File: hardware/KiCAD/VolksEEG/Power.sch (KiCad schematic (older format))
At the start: 43 parts, among them U4 LM2660MX, U5 TPS78425Q

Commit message: Updated schem symbol for ADP7182.
Converted symbol to be more KiCAD-like.
This includes stacking the pins, removing the NC pins, and making the background yellow.
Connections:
- wire segments 160 -> 155
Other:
- moved on the sheet: C8, C9, C?, U?

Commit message: Fixed an bug with the global power nets being used.
The use of global power nets caused the +3V3A, +3V3, and -3V3A nets to be shorted together.
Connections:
- net labels removed: VDD
- wire segments 155 -> 148
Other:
- note added: "LV and FC need jumpers"
- note added: "What are these for?"

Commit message: Updated schem symbols on Power sheet.
Updated symbols to remove NC pins.
Updated pcb footprints to use default SOT-23-5 rather than custom footprint, and deleted custom footprint.
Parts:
- removed C?: 10n, Capacitor_SMD:C_0603_1608Metric_Pad1.08x0.95mm_HandSolder, symbol Device:C
- removed U5: TPS78425Q, VolksEEG:SOT95P280X145-5N, symbol VolksEEG:TPS78425Q
- removed U?: LP3990MF-3.3, VolksEEG:SOT95P280X145-5N, symbol VolksEEG:LP3990MF-3.3
- added JP?: Jumper_NC_Small, symbol Device:Jumper_NC_Small
- added JP?: Jumper_NO_Small, symbol Device:Jumper_NO_Small
- added U?: LP3990MF-3.3, Package_TO_SOT_SMD:SOT-23-5_HandSoldering, symbol VolksEEG:LP3990MF-3.3
- added U?: TPS78425Q, Package_TO_SOT_SMD:SOT-23-5_HandSoldering, symbol VolksEEG:TPS78425Q
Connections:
- net +3V3: now also U?.5 (OUT)
- net +3V3A: now also JP?.2, U?.1 (IN), U?.3 (EN)
- net +5V: now also U?.1 (IN), U?.3 (EN)
- net GNDA: now also JP?.2, U?.2 (GND)
- net GNDD: now also U?.2 (GND)
- net at U4.1 (FC): now also JP?.1
- net at U4.6 (LV): now also JP?.1
- net at C8.1, C?.1, L?.1: now also U?.5 (OUT)
- net VDDA renamed +2V5
- net VSSA renamed -2V5
- no-connect marks 4 -> 1
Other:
- note removed: "LV and FC need jumpers"
- moved on the sheet: C2, C?, L?, U4

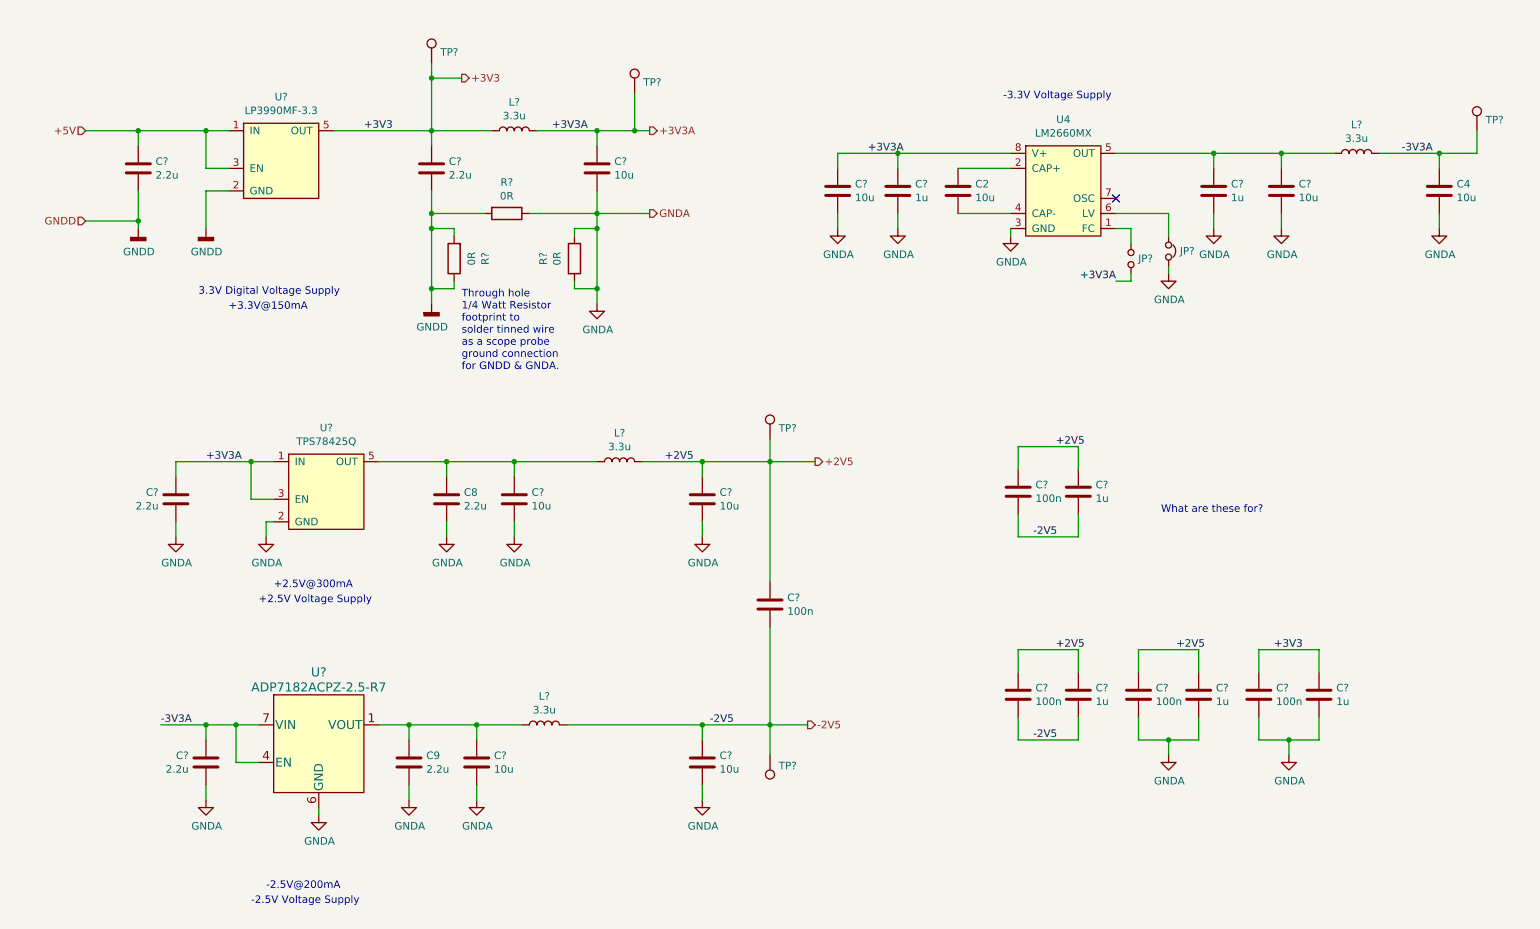
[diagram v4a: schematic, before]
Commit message: Removed custom global power symbols to prevent the bug from happening again.
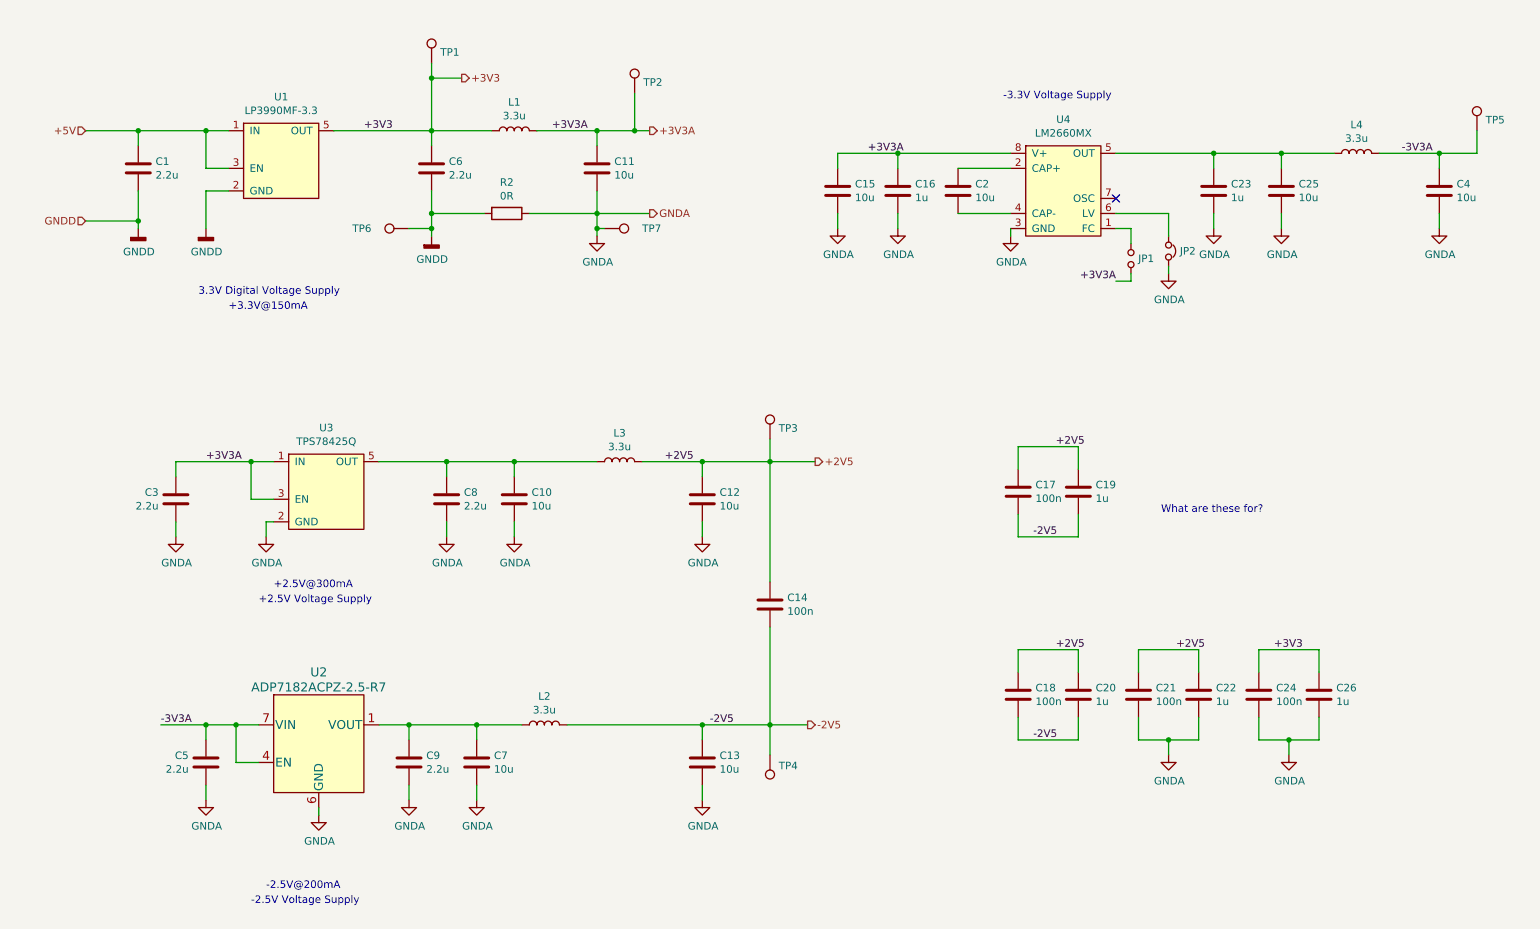
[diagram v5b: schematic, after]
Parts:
- removed R? (x2): 0R, symbol Device:R
- added TP6, TP7: +3V3A, symbol Connector:TestPoint
- gave numbers to parts that had none: 37
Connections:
- net GNDA: now also TP7.1
- net GNDD: now also TP6.1
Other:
- note removed: "Through hole \n1/4 Watt Resistor \nfootprint to \nsolder tinned wire \nas a scope probe \nground connection\nfor GNDD & GNDA."

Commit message: Annotated schematic and cleared ERC errors.
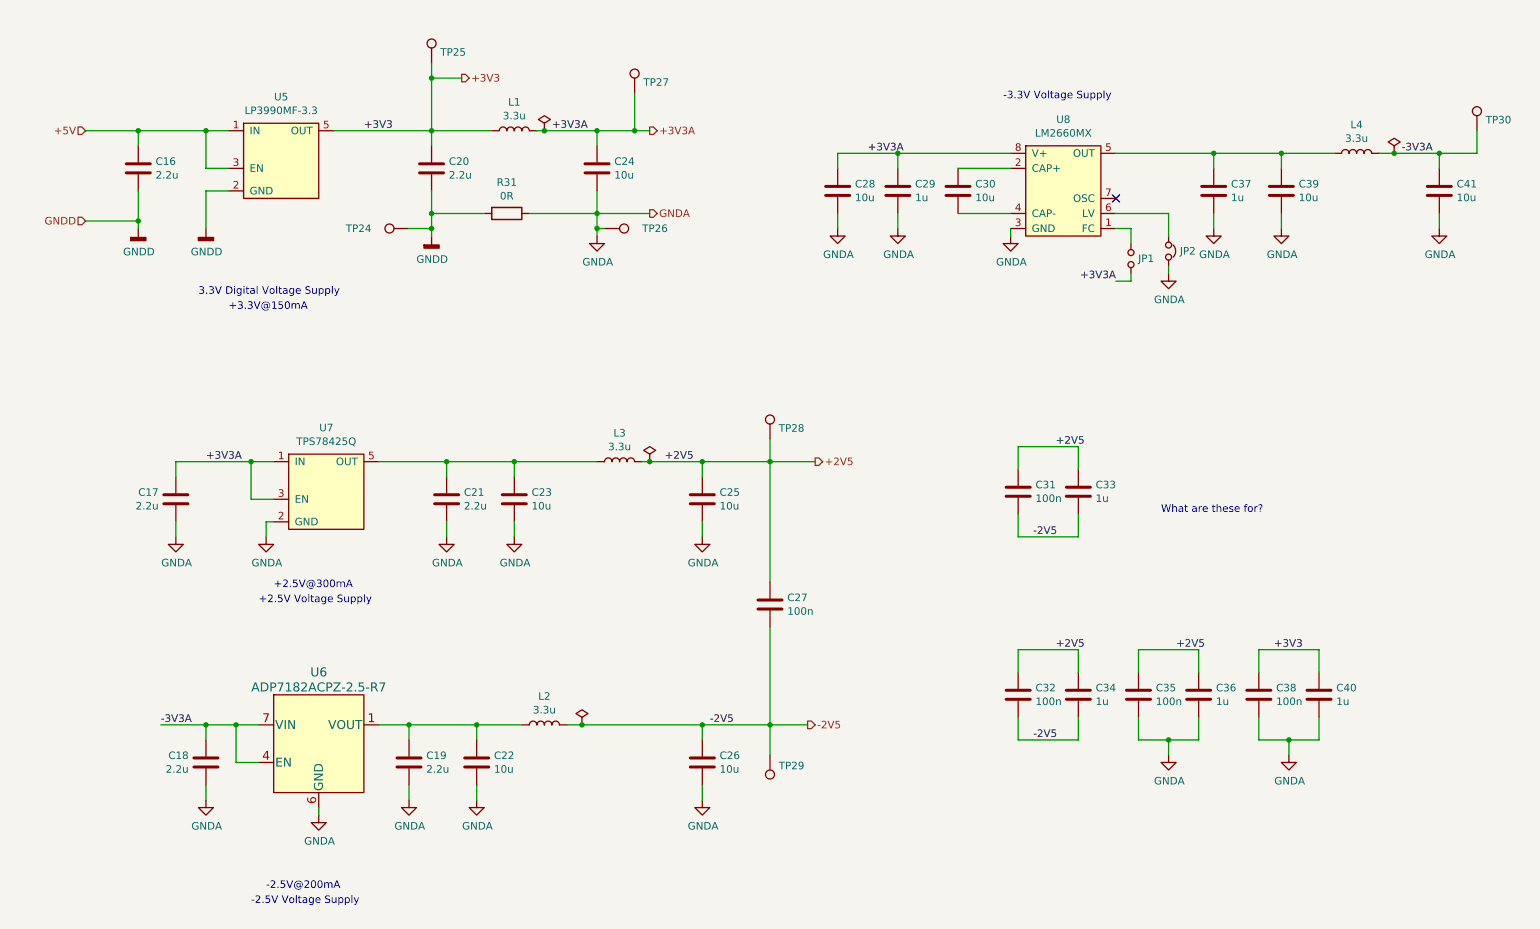
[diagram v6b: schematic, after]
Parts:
- renumbered C1 to C16, C3 to C17, C5 to C18, C9 to C19, C6 to C20, C8 to C21, C7 to C22, C10 to C23, C11 to C24, C12 to C25, C13 to C26, C14 to C27, C15 to C28, C16 to C29, C2 to C30, C17 to C31, C18 to C32, C19 to C33, C20 to C34, C21 to C35, C22 to C36, C23 to C37, C24 to C38, C25 to C39, C26 to C40, C4 to C41, R2 to R31, TP6 to TP24, TP1 to TP25, TP7 to TP26, TP2 to TP27, TP3 to TP28, TP4 to TP29, TP5 to TP30, U1 to U5, U2 to U6, U3 to U7, U4 to U8

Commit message: General schematic cleanup, and assigning some footprints.
Cleaning up the meta-data within KiCAD, and assigning some basic footprints.
Also, cleaning out some footprint references that didn't point anywhere.
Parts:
- JP1: footprint (none) -> Jumper:SolderJumper-2_P1.3mm_Open_Pad1.0x1.5mm
- JP2: footprint (none) -> Jumper:SolderJumper-2_P1.3mm_Bridged_Pad1.0x1.5mm
- R31: footprint (none) -> Resistor_SMD:R_0603_1608Metric_Pad0.98x0.95mm_HandSolder
- TP24, TP26: value +3V3A -> TestPoint; footprint (none) -> TestPoint:TestPoint_Keystone_5010-5014_Multipurpose
- TP25: value VDD_+3V3 -> TestPoint
- TP27: value +3V3A -> TestPoint
- TP28: value +2V5 -> TestPoint
- TP29: value -2V5 -> TestPoint
- TP30: value -3V3A -> TestPoint
- U6: footprint CP_8_11_ADI -> (none)
- U7: Suppler 1 Link https://www.digikey.com/en/products/detail/texas-instrument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 -> (none); Suppler 2 Link https://eu.mouser.com/ProductDetail/Texas-Instruments/TPS78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 -> (none); Supplier 1 Link (none) -> https://www.digikey.com/en/products/detail/texas-instrument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; Supplier 2 Link (none) -> https://eu.mouser.com/ProductDetail/Texas-Instruments/TPS78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
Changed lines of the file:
@@
 F 0 "R31" V 4093 1850 50  0000 C CNN
 F 1 "0R" V 4184 1850 50  0000 C CNN
-F 2 "" V 4230 1850 50  0001 C CNN
+F 2 "Resistor_SMD:R_0603_1608Metric_Pad0.98x0.95mm_HandSolder" V 4230 1850 50  0001 C CNN
 F 3 "~" H 4300 1850 50  0001 C CNN
 	1    4300 1850
@@
 P 5150 1050
 F 0 "TP27" H 5208 1122 50  0000 L CNN
-F 1 "+3V3A" H 5208 1077 50  0001 L CNN
+F 1 "TestPoint" H 5208 1077 50  0001 L CNN
 F 2 "" H 5350 1050 50  0001 C CNN
 F 3 "~" H 5350 1050 50  0001 C CNN
@@
 P 10750 1300
 F 0 "TP30" H 10808 1372 50  0000 L CNN
-F 1 "-3V3A" H 10808 1327 50  0001 L CNN
+F 1 "TestPoint" H 10808 1327 50  0001 L CNN
 F 2 "" H 10950 1300 50  0001 C CNN
 F 3 "~" H 10950 1300 50  0001 C CNN
@@
 P 6050 3350
 F 0 "TP28" H 6108 3422 50  0000 L CNN
-F 1 "+2V5" H 6108 3377 50  0001 L CNN
+F 1 "TestPoint" H 6108 3377 50  0001 L CNN
 F 2 "" H 6250 3350 50  0001 C CNN
 F 3 "~" H 6250 3350 50  0001 C CNN
@@
 P 6050 5450
 F 0 "TP29" H 5992 5522 50  0000 R CNN
-F 1 "-2V5" H 6108 5477 50  0001 L CNN
+F 1 "TestPoint" H 6108 5477 50  0001 L CNN
 F 2 "" H 6250 5450 50  0001 C CNN
 F 3 "~" H 6250 5450 50  0001 C CNN
@@
 F 0 "U6" H 3050 5800 60  0000 C CNN
 F 1 "ADP7182ACPZ-2.5-R7" H 3050 5700 60  0000 C CNN
-F 2 "CP_8_11_ADI" H 3850 5690 60  0001 C CNN
+F 2 "" H 3850 5690 60  0001 C CNN
 F 3 "" H 3050 5350 60  0000 C CNN
 	1    3050 5350
@@
 P 3800 850
 F 0 "TP25" H 3858 922 50  0000 L CNN
-F 1 "VDD_+3V3" H 3858 877 50  0001 L CNN
+F 1 "TestPoint" H 3858 877 50  0001 L CNN
 F 2 "" H 4000 850 50  0001 C CNN
 F 3 "~" H 4000 850 50  0001 C CNN
@@
 F 2 "Package_TO_SOT_SMD:SOT-23-5_HandSoldering" H 3450 3300 50  0001 C CNN
 F 3 "https://www.ti.com/lit/gpn/tps784-q1" H 3100 3700 50  0001 C CNN
-F 4 "https://www.digikey.com/en/products/detail/texas-instruments/TPS78425QDBVRQ1/13563001" H 3600 3150 50  0001 C CNN "Suppler 1 Link"
-F 5 "https://eu.mouser.com/ProductDetail/Texas-Instruments/TPS78425QDBVRQ1?qs=81r%252BiQLm7BRHMcAKEdEeyg%3D%3D" H 3600 3250 50  0001 C CNN "Suppler 2 Link"
+F 4 "https://www.digikey.com/en/products/detail/texas-instruments/TPS78425QDBVRQ1/13563001" H 0   0   50  0001 C CNN "Supplier 1 Link"
+F 5 "https://eu.mouser.com/ProductDetail/Texas-Instruments/TPS78425QDBVRQ1?qs=81r%252BiQLm7BRHMcAKEdEeyg%3D%3D" H 0   0   50  0001 C CNN "Supplier 2 Link"
 	1    3100 3700
 	1    0    0    -1
@@
 F 0 "JP2" V 8700 2175 50  0000 L CNN
 F 1 "Jumper_NC_Small" V 8745 2174 50  0001 L CNN
-F 2 "" H 8700 2100 50  0001 C CNN
+F 2 "Jumper:SolderJumper-2_P1.3mm_Bridged_Pad1.0x1.5mm" H 8700 2100 50  0001 C CNN
 F 3 "~" H 8700 2100 50  0001 C CNN
 	1    8700 2100
@@
 F 0 "JP1" V 8450 2198 50  0000 L CNN
 F 1 "Jumper_NO_Small" V 8495 2198 50  0001 L CNN
-F 2 "" H 8450 2150 50  0001 C CNN
+F 2 "Jumper:SolderJumper-2_P1.3mm_Open_Pad1.0x1.5mm" H 8450 2150 50  0001 C CNN
 F 3 "~" H 8450 2150 50  0001 C CNN
 	1    8450 2150
@@
 P 3650 1950
 F 0 "TP24" V 3650 2200 50  0000 L CNN
-F 1 "+3V3A" H 3708 1977 50  0001 L CNN
-F 2 "" H 3850 1950 50  0001 C CNN
+F 1 "TestPoint" H 3708 1977 50  0001 L CNN
+F 2 "TestPoint:TestPoint_Keystone_5010-5014_Multipurpose" H 3850 1950 50  0001 C CNN
 F 3 "~" H 3850 1950 50  0001 C CNN
 	1    3650 1950
@@
 P 4950 1950
 F 0 "TP26" V 4950 2200 50  0000 L CNN
-F 1 "+3V3A" H 5008 1977 50  0001 L CNN
-F 2 "" H 5150 1950 50  0001 C CNN
+F 1 "TestPoint" H 5008 1977 50  0001 L CNN
+F 2 "TestPoint:TestPoint_Keystone_5010-5014_Multipurpose" H 5150 1950 50  0001 C CNN
 F 3 "~" H 5150 1950 50  0001 C CNN
 	1    4950 1950

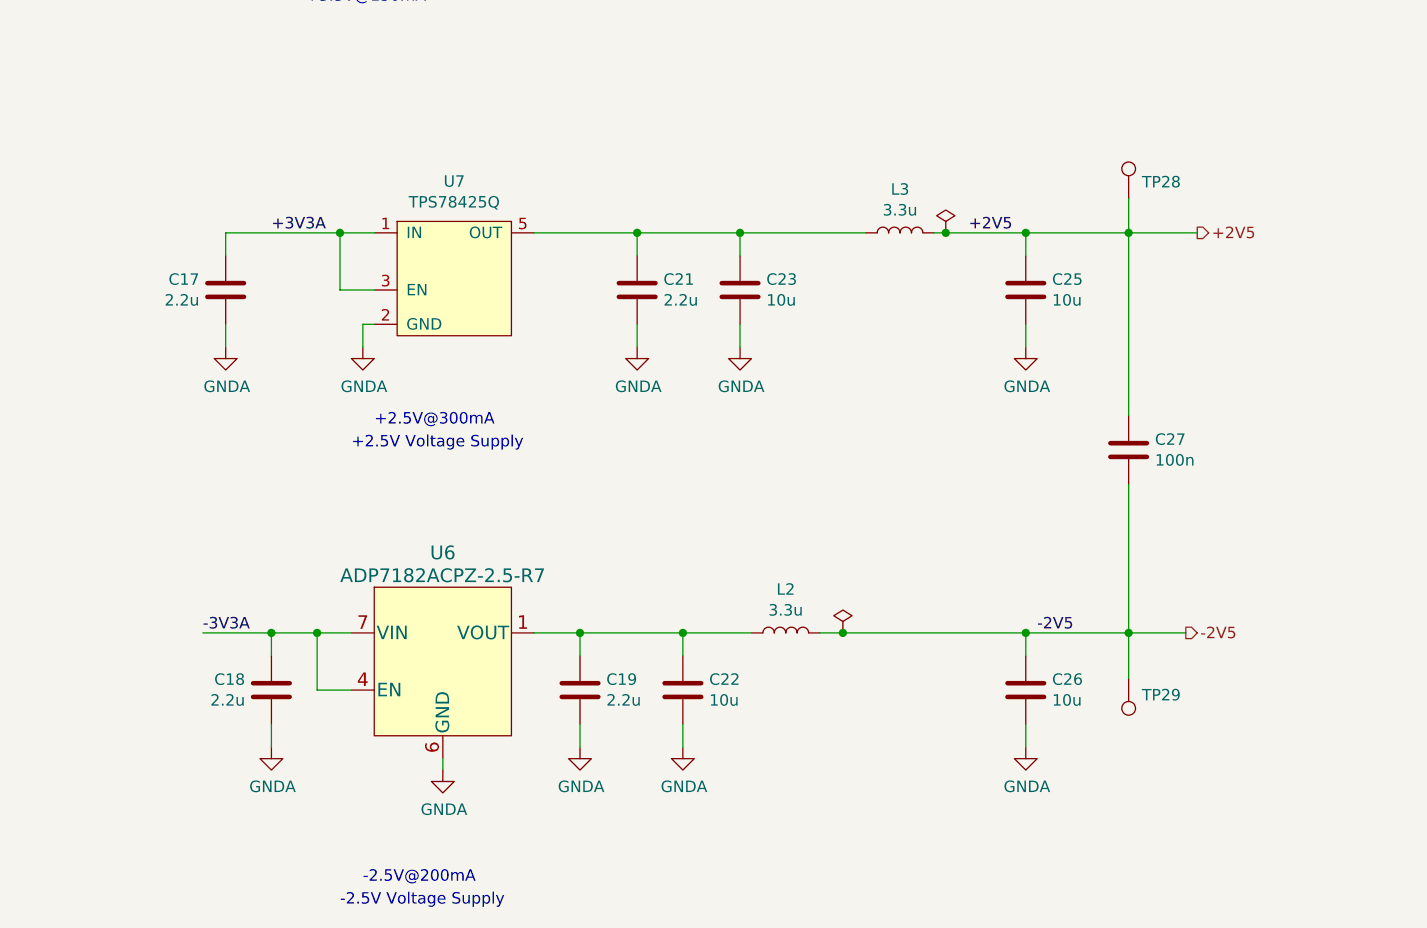
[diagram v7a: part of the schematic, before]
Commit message: Change ADS1299 over to using the KiCAD library footprint.
Also deleted the custom drawn QFP footprint.
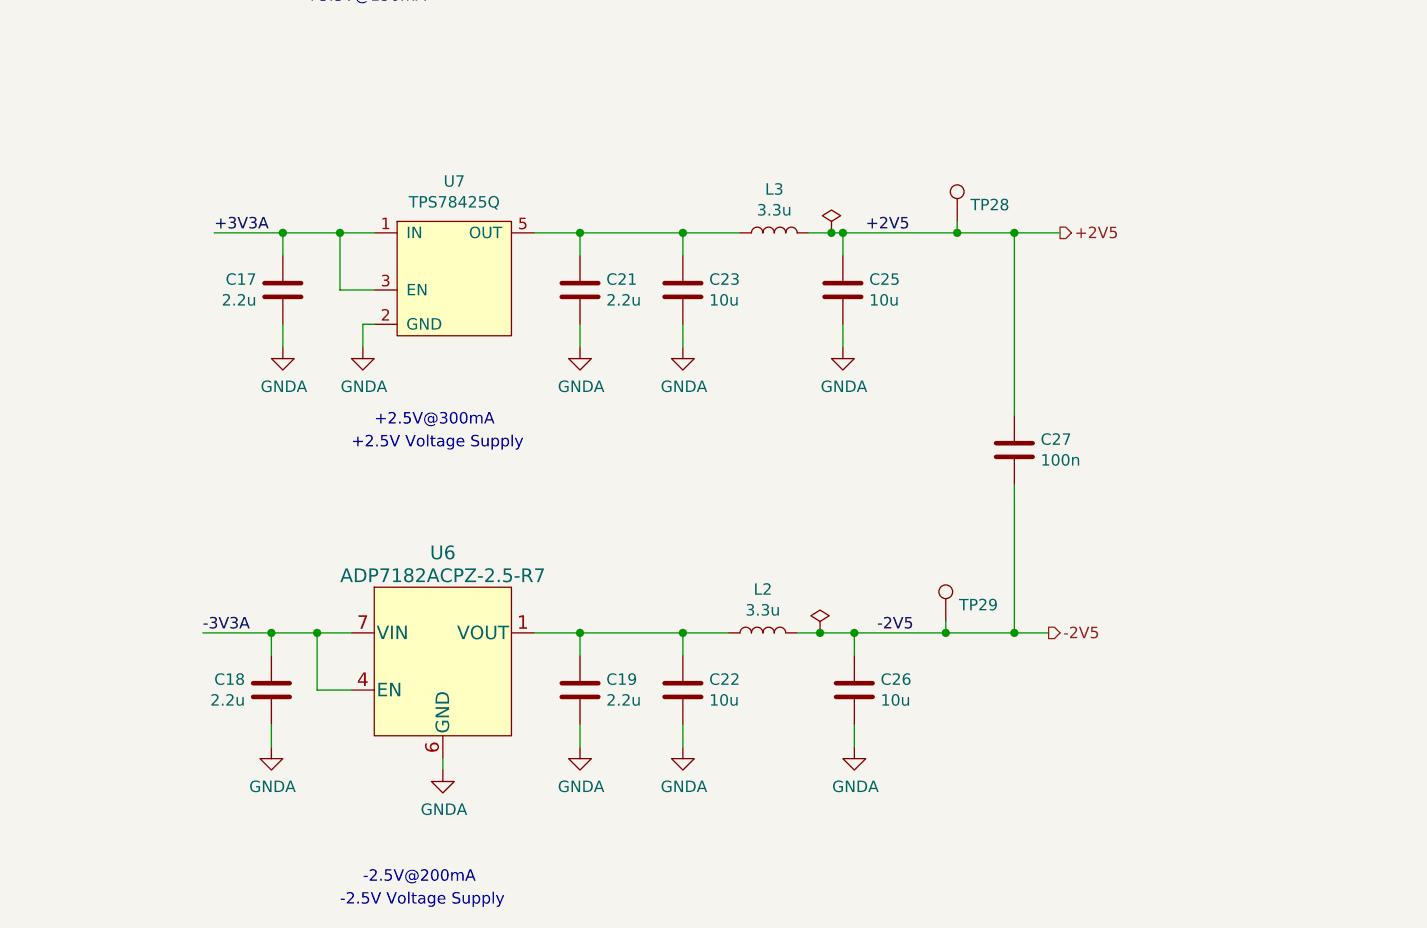
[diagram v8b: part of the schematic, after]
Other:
- moved on the sheet: C17, C21, C23, C25, C26, C27, L2, L3, TP28, TP29
